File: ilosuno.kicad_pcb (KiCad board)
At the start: 2 copper layers, 43.6 x 39.5 mm, 45 parts, among them J1 UNPOPULATED_2.54MM_PADS, J2 KF350, J3 UNPOPULATED_2.54MM_PADS, J4 KF350, Q1 IRLR7843TRPBF, Q2 AO3400A, Q3 AO3400A, Q4 IRLR7843TRPBF, Q5 AO3400A, Q6 IRLR7843TRPBF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

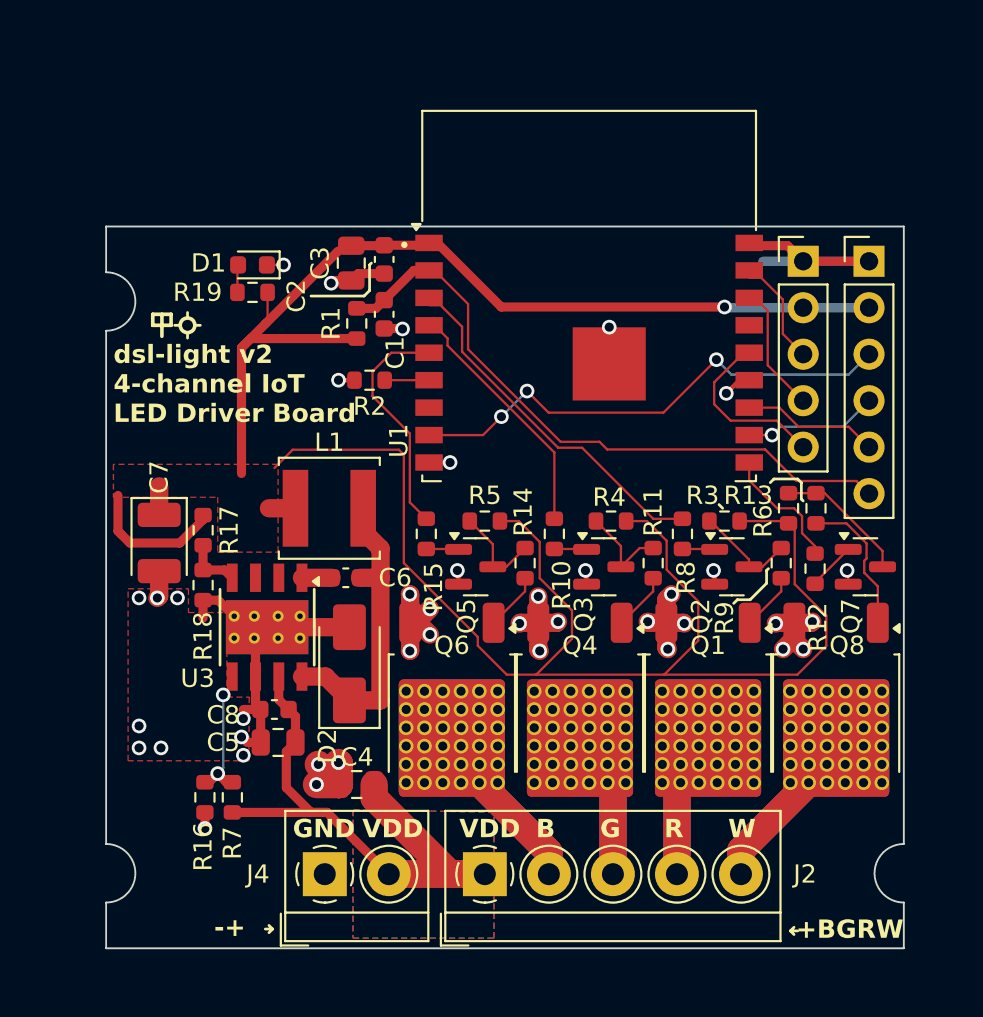
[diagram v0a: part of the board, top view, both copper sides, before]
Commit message: rev1a: Fixed buck converter output overvoltage bug. Added reverse polarity protection. Exposed more pins to GPIO header (RST, IO2 and IO15)
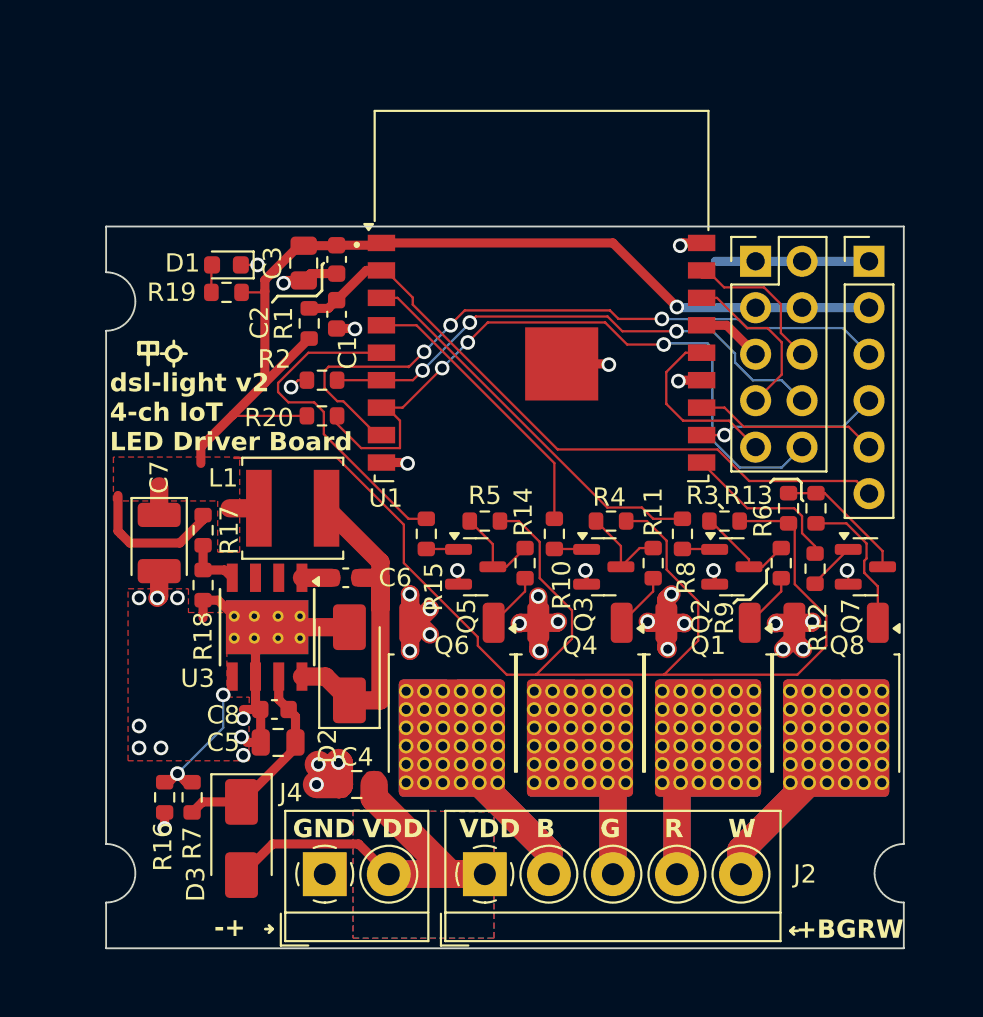
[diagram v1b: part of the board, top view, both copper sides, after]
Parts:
- added D3: SS54/SMA, Diode_SMD:D_SMA, F.Cu at (117.4, 105.2)
- added R20: 10k, Resistor_SMD:R_0603_1608Metric, F.Cu at (121.8, 82.2)
- J1: value UNPOPULATED_2.54MM_PADS -> 2.54MM_PADS
- J3: value UNPOPULATED_2.54MM_PADS -> 2.54MM_PADS; footprint Connector_PinHeader_2.54mm:PinHeader_1x05_P2.54mm_Vertical -> Connector_PinHeader_2.54mm:PinHeader_2x05_P2.54mm_Vertical
- L1: value 68uH/SWPA5040S680MT -> 100uH/SWPA5040S101MT
- R18: value 5.6k -> 6k49
- moved G*** 7.74 mm to (130.1, 82.2)
- moved C1 2.60 mm to (122.6, 76.6)
- moved C2 2.60 mm to (122.6, 73.6)
- moved C3 2.60 mm to (120.8, 73.8)
- moved R1 2.60 mm to (121.1, 77.1)
- moved R2 2.60 mm to (121.8, 80.2)
- moved J3 2.60 mm to (145.5, 73.7)
- moved U1 2.60 mm to (133.8, 78.7)
- moved R16 2.20 mm to (113.2, 103.0)
- moved R7 2.20 mm to (114.7, 103.0)
- moved L1 2.00 mm to (120.2, 87.2)
- moved D1 1.42 mm to (116.6, 73.9)
- moved R19 1.42 mm to (116.6, 75.4)
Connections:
- C5 pad 1: VDD -> Net-(D3-K)
- C8 pad 1: VDD -> Net-(D3-K)
- J3 pad 2: +3V3 -> GND
- J3 pad 3: IO16 -> +3V3
- J3 pad 4: IO6 -> +3V3
- J3 pad 5: IO5 -> RST
- R2 pad 1: Net-(U1-IO15) -> IO15
- R7 pad 1: VDD -> Net-(D3-K)
- U1 pad 15: unconnected-(U1-RST-Pad15) -> RST
- U1 pad 16: IO6 -> TOUT
- U1 pad 6: Net-(U1-IO15) -> IO15
- U1 pad 7: unconnected-(U1-IO2-Pad7) -> IO2
- U3 pad 7: VDD -> Net-(D3-K)
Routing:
- net IO2: track 0.00 -> 39.3 mm, vias 0 -> 3
- net IO15: track 0.00 -> 29.1 mm, vias 0 -> 3
- net Net-(D3-K): track 0.00 -> 11.4 mm
- net IO0: track 27.5 -> 37.6 mm
- net VDD: track 38.4 -> 28.4 mm
- net TOUT: track 0.00 -> 9.16 mm
- net IO6: track 7.02 -> 0.00 mm
- net CH_B: track 12.8 -> 18.5 mm
- net RST: track 0.00 -> 3.60 mm
- net +3V3: track 136.3 -> 139.0 mm
- net ESP_RX: track 7.33 -> 9.93 mm
- net ESP_TX: track 7.44 -> 10.0 mm
- net GND: track 69.8 -> 67.2 mm, vias 40 -> 41
- net Net-(D2-K): track 16.9 -> 19.3 mm
- net CH_W: track 6.62 -> 9.04 mm
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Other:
- board text added: "12~24V 10A MAX POWER IN"
- board text added: "15"
- board text added: "2"
- board text added: "D4"
- board text added: "D8"
- board text added: "DISCLAIMER: THIS DEVICE IS A PROTOTYPE AND"
- board text added: "HAS NOT BEEN TESTED FOR HIGHER POWER LOAD."
- board text added: "PCB Designed by Sadale for DSL"
- board text added: "PCB rev1a"
- board text added: "RST"
- board text added: "TOUT"
- board text added: "To boot:"
- board text added: "USE IT AT YOUR OWN RISK! DO NOT GET YOUR HOUSE BURNED DOWN!"
- board text added: "based on Lionello's 3ch design"
- board text added: "dsl-light v2 4-ch IoT LED Driver Board"
- board text added: "ilo suno"
- board text added: "must high/NC"
- board text added: "must low"
- board text removed: "12~24V POWER IN"
- board text removed: "6"
- board text removed: "PCB rev0g"
- board text removed: "dsl-light v2 4-channel IoT LED Driver Board PCB Designed by Sadale for Dimsumlabs based on Lionello's 3-ch design DISCLAIMER: THIS DEVICE IS A PROTOTYPE AND HAS NOT BEEN TESTED FOR HIGHER POWER LOAD. USE IT AT YOUR OWN RISK! DO NOT GET YOUR HOUSE BURNED DOWN!"

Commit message: rev1b: Corrected silk mark in regard to the required initial boot pin state, with on-board pull-down considered
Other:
- board text added: "PCB rev1b"
- board text added: "must low/NC"
- board text removed: "PCB rev1a"
- board text removed: "must low"
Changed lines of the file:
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@@
 		)
 	)
-	(gr_text "must low"
+	(gr_text "must low/NC"
 		(at 142.2 95.65 0)
 		(layer "B.SilkS")
@@
 		)
 	)
-	(gr_text "PCB rev1a"
+	(gr_text "PCB rev1b"
 		(at 119 110.35 0)
 		(layer "B.SilkS")
